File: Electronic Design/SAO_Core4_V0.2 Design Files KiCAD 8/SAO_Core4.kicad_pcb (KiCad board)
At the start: 2 copper layers, 50.8 x 63.5 mm, 92 parts, among them Q1 MMBT4403LT1G, Q13 MMBT4403LT1G, Q14 MMBT4401LT1G, Q17 MMBT4403LT1G, Q18 MMBT4401LT1G, Q2 MMBT4401LT1G, Q21 Q_NMOS_DGS_AO3400A, Q22 SL3401A, Q3 MMBT4403LT1G, Q4 MMBT4401LT1G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

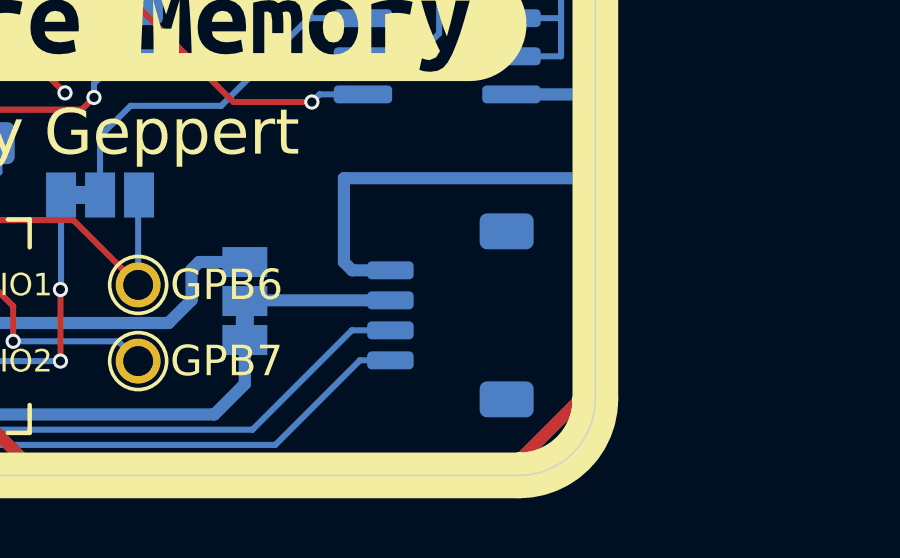
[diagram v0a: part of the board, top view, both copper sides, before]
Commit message: Clean-up schematic DRC
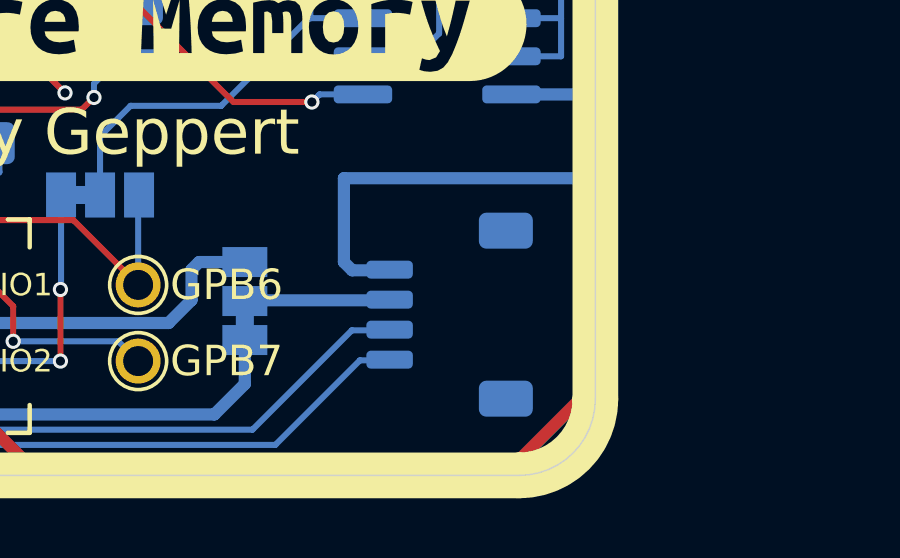
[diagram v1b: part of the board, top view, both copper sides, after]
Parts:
- removed X9: QWIIC, Connector_JST:JST_SH_SM04B-SRSS-TB_1x04-1MP_P1.00mm_Horizontal
- added X3: QWIIC, Connector_JST:JST_SH_SM04B-SRSS-TB_1x04-1MP_P1.00mm_Horizontal, B.Cu at (128.1, 152.2)

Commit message: Begin refinements for HWV0.2.0
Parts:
- removed kibuzzard-66BCB8D2: G***, kibuzzard-66BCB8D2
- removed kibuzzard-66C119C9: G***, kibuzzard-66C119C9
- added kibuzzard-66D35F07: G***, kibuzzard-66D35F07, F.Cu at (94.6, 151.0)
- added kibuzzard-66D35F61: G***, kibuzzard-66D35F61, F.Cu at (107.5, 142.6)
- moved L2 32.3 mm to (121.0, 151.2)
- moved L1 7.27 mm to (113.3, 110.1)
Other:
- board text added: "0x20-27 (default 27)"
- board text added: "SAO Contest Size 2x1.5inch"
- board text added: "SAO RX"
- board text added: "SAO TX"
